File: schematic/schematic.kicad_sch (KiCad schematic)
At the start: 3 parts, among them U1 ESP32-WROOM-32

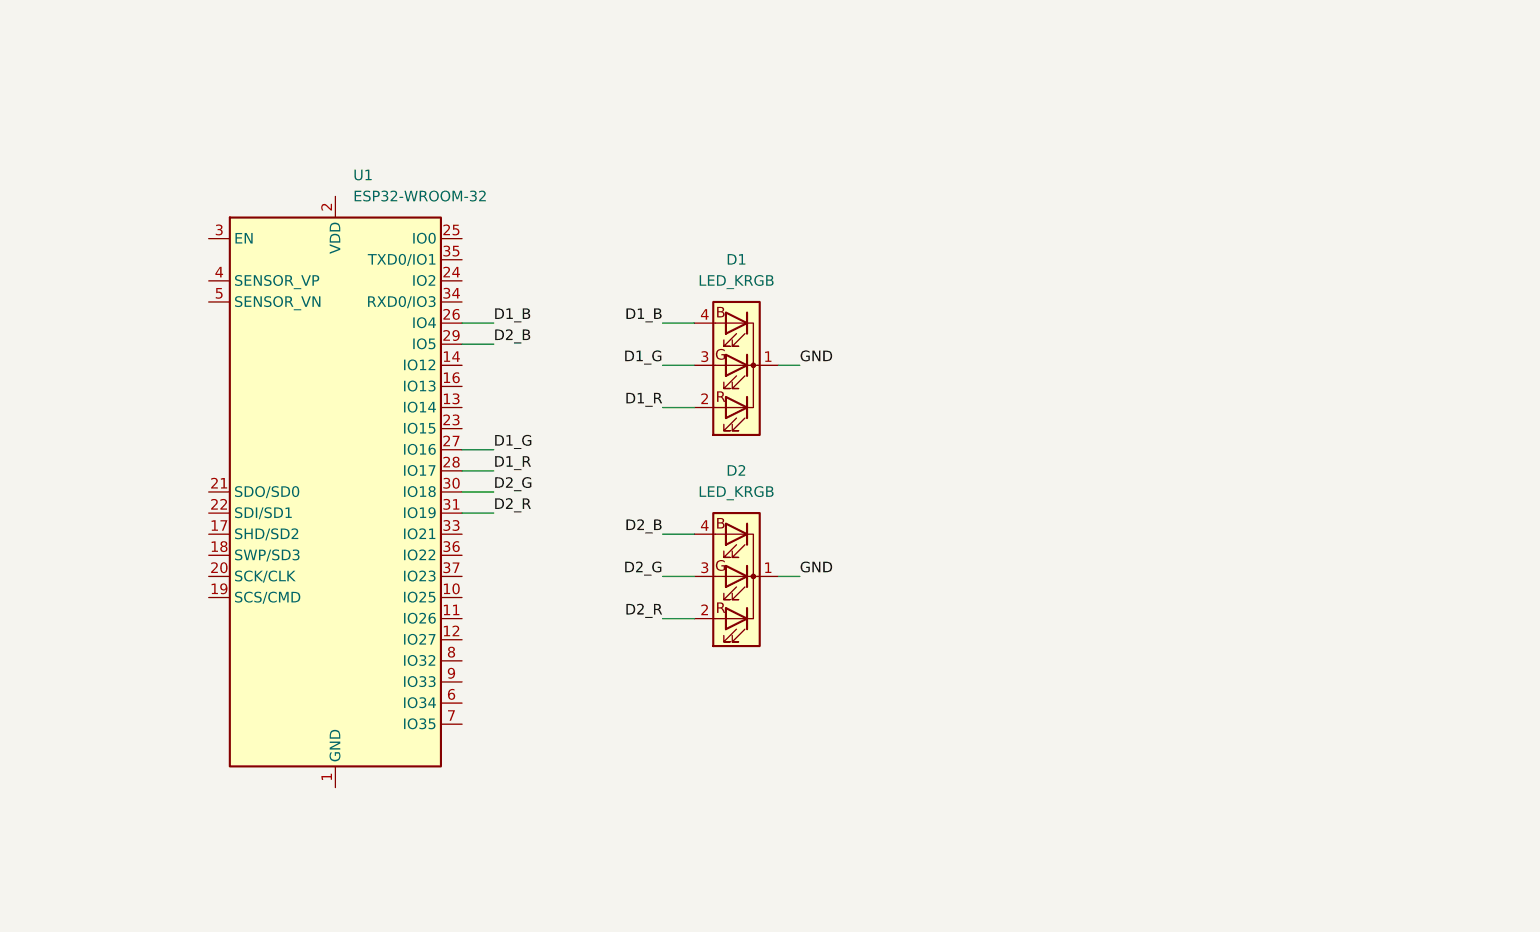
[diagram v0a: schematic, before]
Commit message: feat(schematic): add motors, RES, moisture sensors
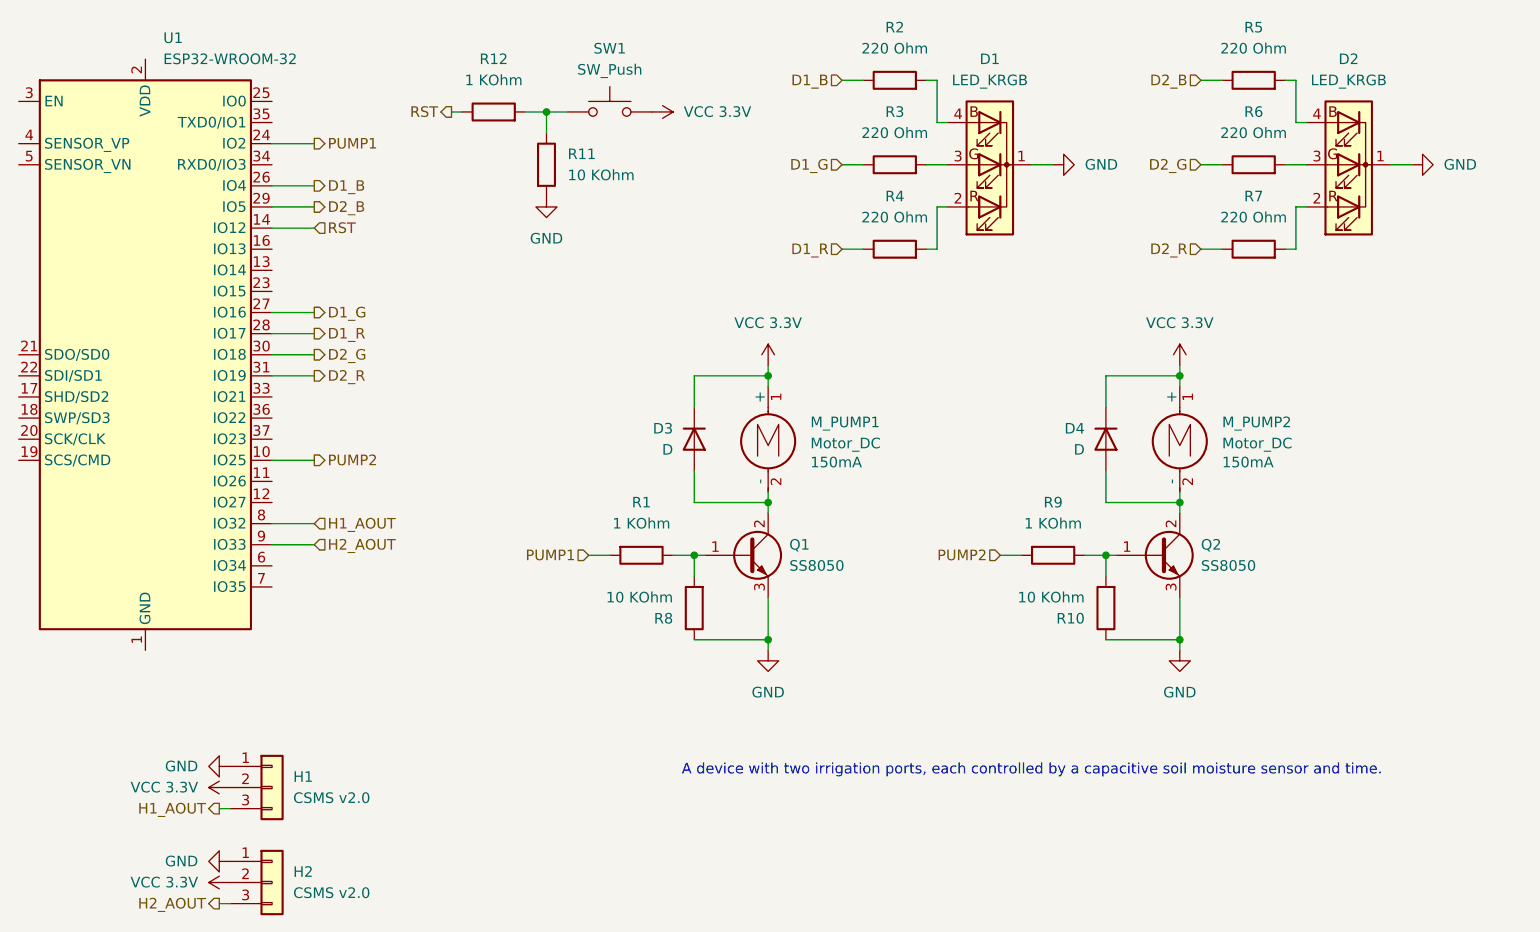
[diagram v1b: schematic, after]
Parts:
- added D3, D4: D, symbol Device:D
- added H1, H2: CSMS v2.0, symbol Connector_Generic:Conn_01x03
- added M_PUMP1, M_PUMP2: Motor_DC, symbol Motor:Motor_DC
- added Q1, Q2: SS8050, symbol Transistor_BJT:Q_NPN_BCE
- added R1, R12, R9: 1 KOhm, symbol Device:R
- added R10, R11, R8: 10 KOhm, symbol Device:R
- added R2, R3, R4, R5, R6, R7: 220 Ohm, symbol Device:R
- added SW1: SW_Push, symbol Switch:SW_Push
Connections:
- net D1_B: now also R2.1; no longer D1.4 (BA)
- net D1_G: now also R3.1; no longer D1.3 (GA)
- net D1_R: now also R4.1; no longer D1.2 (RA)
- net D2_B: now also R5.1; no longer D2.4 (BA)
- net D2_G: now also R6.1; no longer D2.3 (GA)
- net D2_R: now also R7.1; no longer D2.2 (RA)
- net GND: now also H1.1 (Pin_1), H2.1 (Pin_1), Q1.3 (E), Q2.3 (E), R10.1, R11.2, R8.1
- net PUMP2: now reaches U1.10 (IO25)
- net PUMP2: now also R9.2
- net RST: now reaches U1.14 (IO12)
- net RST: now also R12.1
- net PUMP1: now reaches U1.24 (IO2)
- net PUMP1: now also R1.2
- net H1_AOUT: now reaches U1.8 (IO32)
- net H1_AOUT: now also H1.3 (Pin_3)
- net H2_AOUT: now reaches U1.9 (IO33)
- net H2_AOUT: now also H2.3 (Pin_3)
- new net: D1.2 (RA), R4.2
- new net: D1.3 (GA), R3.2
- new net: D1.4 (BA), R2.2
- new net: Q2.1 (B), R10.2, R9.1
- new net: D2.4 (BA), R5.2
- new net: D2.2 (RA), R7.2
- new net: D2.3 (GA), R6.2
- new net: Q1.1 (B), R1.1, R8.2
- new net: R11.1, R12.2, SW1.1
- new net: D4.2 (A), M_PUMP2.2 (-), Q2.2 (C)
- new net: D3.2 (A), M_PUMP1.2 (-), Q1.2 (C)
- new net VCC 3.3V: D3.1 (K), D4.1 (K), H1.2 (Pin_2), H2.2 (Pin_2), M_PUMP1.1 (+), M_PUMP2.1 (+), SW1.2
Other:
- note added: "A device with two irrigation ports, each controlled by a capacitive soil moisture sensor and time."
- moved on the sheet: D1, D2, U1

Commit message: feat(schematic/fn): migrate to 5V parallel watering
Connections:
- net VCC 3.3V: no longer D3.1 (K), D4.1 (K), M_PUMP1.1 (+), M_PUMP2.1 (+)
- new net VCC 5V: D3.1 (K), D4.1 (K), M_PUMP1.1 (+), M_PUMP2.1 (+)
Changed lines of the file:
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@@
 			)
 		)
-		(property "Value" "VCC 3.3V"
-			(at 157.48 53.34 0)
-			(effects
-				(font
-					(size 1.27 1.27)
-				)
+		(property "Value" "VCC 5V"
+			(at 160.02 57.1499 0)
+			(effects
+				(font
+					(size 1.27 1.27)
+				)
+				(justify left)
 			)
 		)
@@
 			)
 		)
-		(property "Value" "VCC 3.3V"
-			(at 107.95 53.34 0)
-			(effects
-				(font
-					(size 1.27 1.27)
-				)
-			)
-		)
+		(property "Value" "VCC 5V"
+			(at 110.49 57.1499 0)
+			(effects
+				(font
+					(size 1.27 1.27)
+				)
+				(justify left)
+			)
+		)
